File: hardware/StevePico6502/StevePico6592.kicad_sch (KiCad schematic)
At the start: 28 parts, among them J1 Conn_01x16, J2 Conn_01x16, J3 Conn_02x16_Odd_Even, J4 Conn_01x01_Pin, SW1 SW_Push, SW2 SW_Push, U1 65CE02, U2 Pico, U3 74HC595, U4 W65C22NxP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

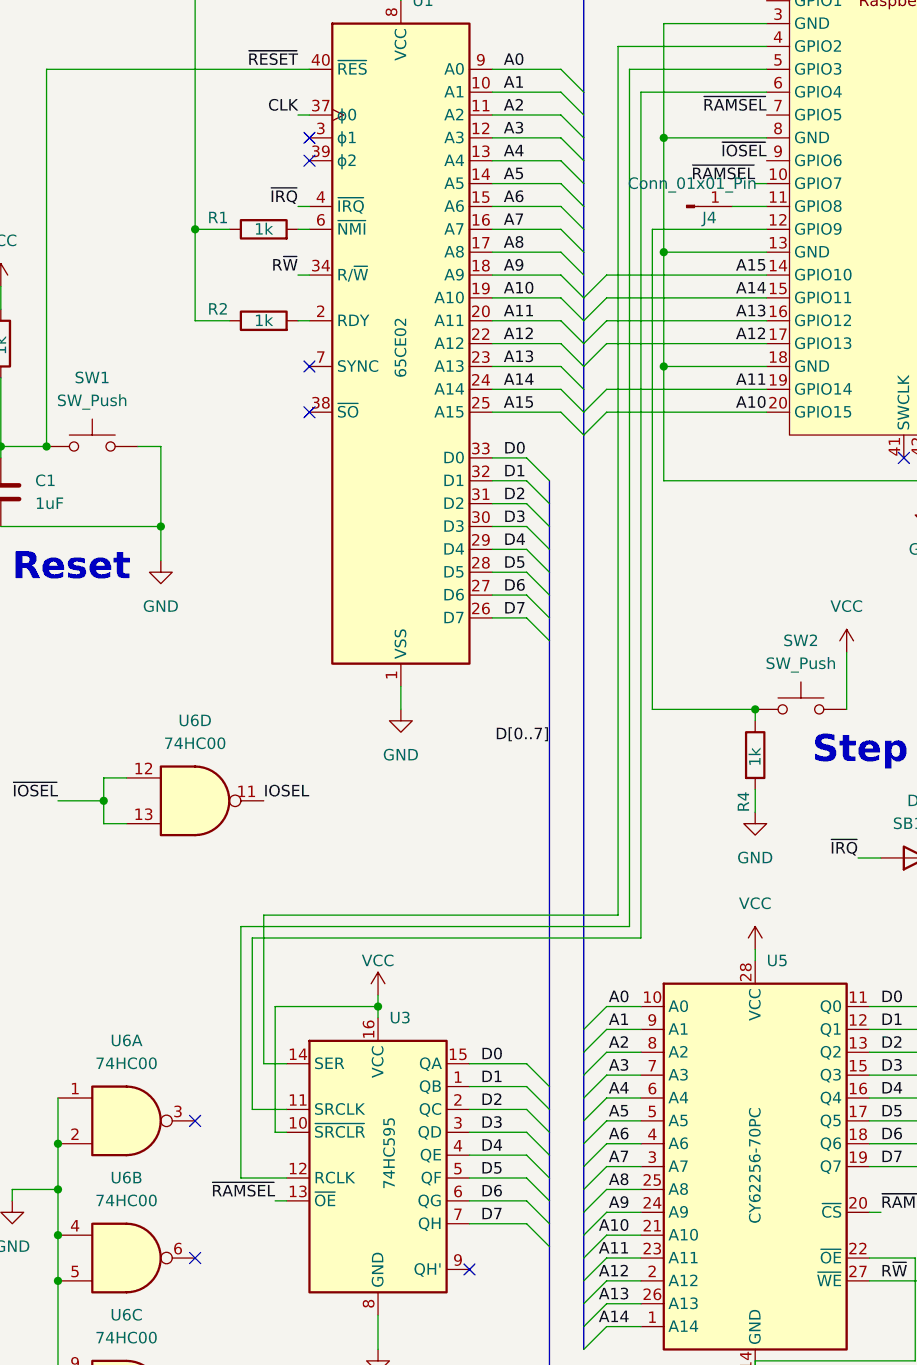
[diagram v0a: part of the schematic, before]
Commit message: fixed bug with dual RAMSEL and no ROMSEL
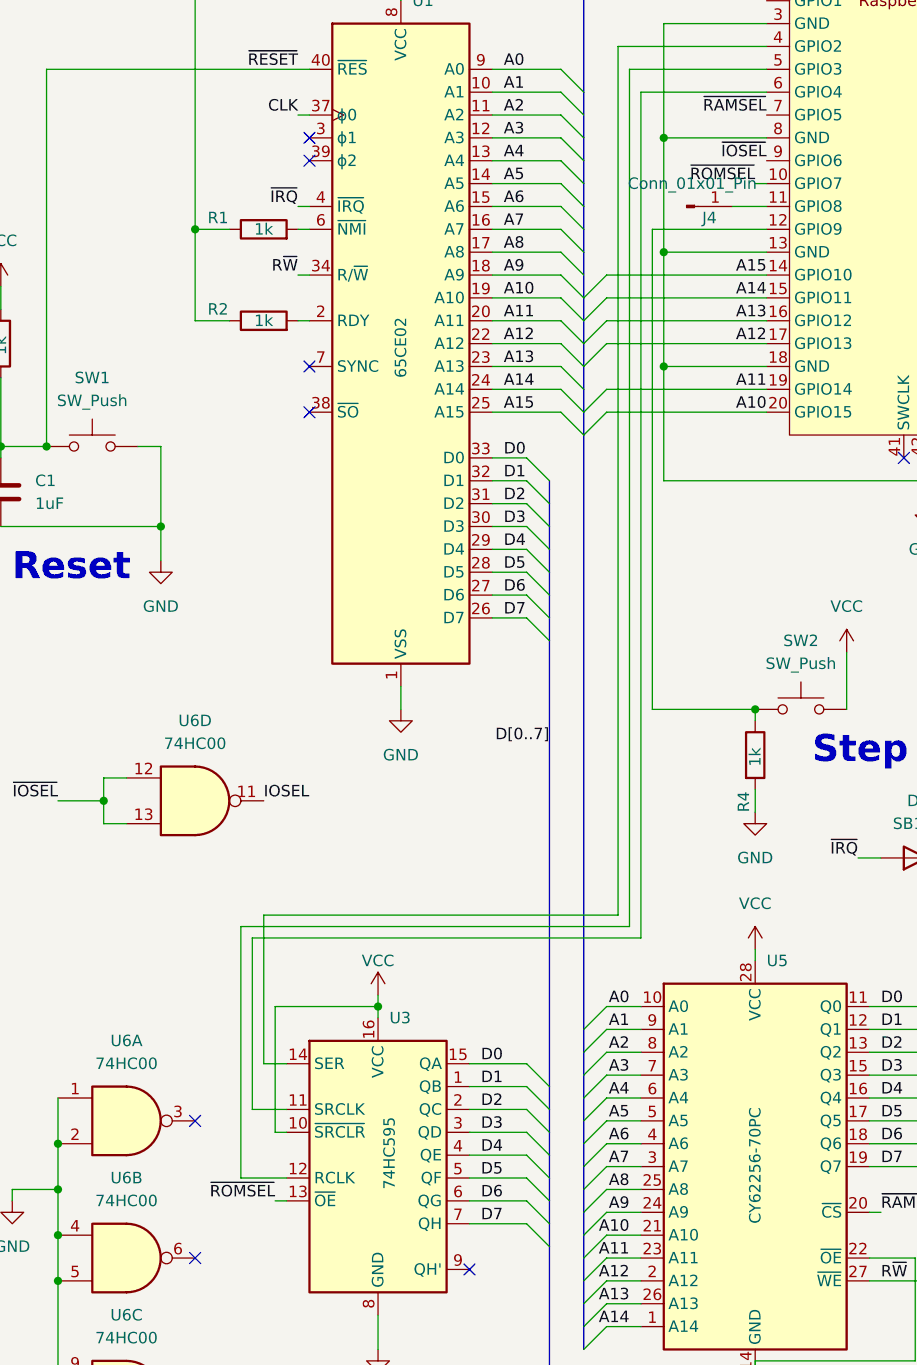
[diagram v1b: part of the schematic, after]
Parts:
- U2: footprint Pi Pico:RPi_Pico_SMD_TH -> MCU_RaspberryPi_and_Boards:RPi_Pico_SMD_TH
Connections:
- net ~{RAMSEL}: no longer U2.10 (GPIO7), U3.13 (~{OE})
- new net ~{ROMSEL}: U2.10 (GPIO7), U3.13 (~{OE})
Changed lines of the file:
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@@
     (effects (font (size 1.27 1.27)) (justify left bottom))
   )
-  (label "~{RAMSEL}" (at 45.72 167.64 180) (fields_autoplaced)
-    (effects (font (size 1.27 1.27)) (justify right bottom))
-  )
-  (label "~{RAMSEL}" (at 99.06 54.61 180) (fields_autoplaced)
+  (label "~{ROMSEL}" (at 45.72 167.64 180) (fields_autoplaced)
+    (effects (font (size 1.27 1.27)) (justify right bottom))
+  )
+  (label "~{ROMSEL}" (at 99.06 54.61 180) (fields_autoplaced)
     (effects (font (size 1.27 1.27)) (justify right bottom))
   )
@@
       (effects (font (size 1.27 1.27)))
     )
-    (property "Footprint" "Pi Pico:RPi_Pico_SMD_TH" (at 118.11 55.88 90)
-      (effects (font (size 1.27 1.27)) hide)
-    )
+    (property "Footprint" "MCU_RaspberryPi_and_Boards:RPi_Pico_SMD_TH" (at 118.11 55.88 90)
+      (effects (font (size 1.27 1.27)) hide)
+    )

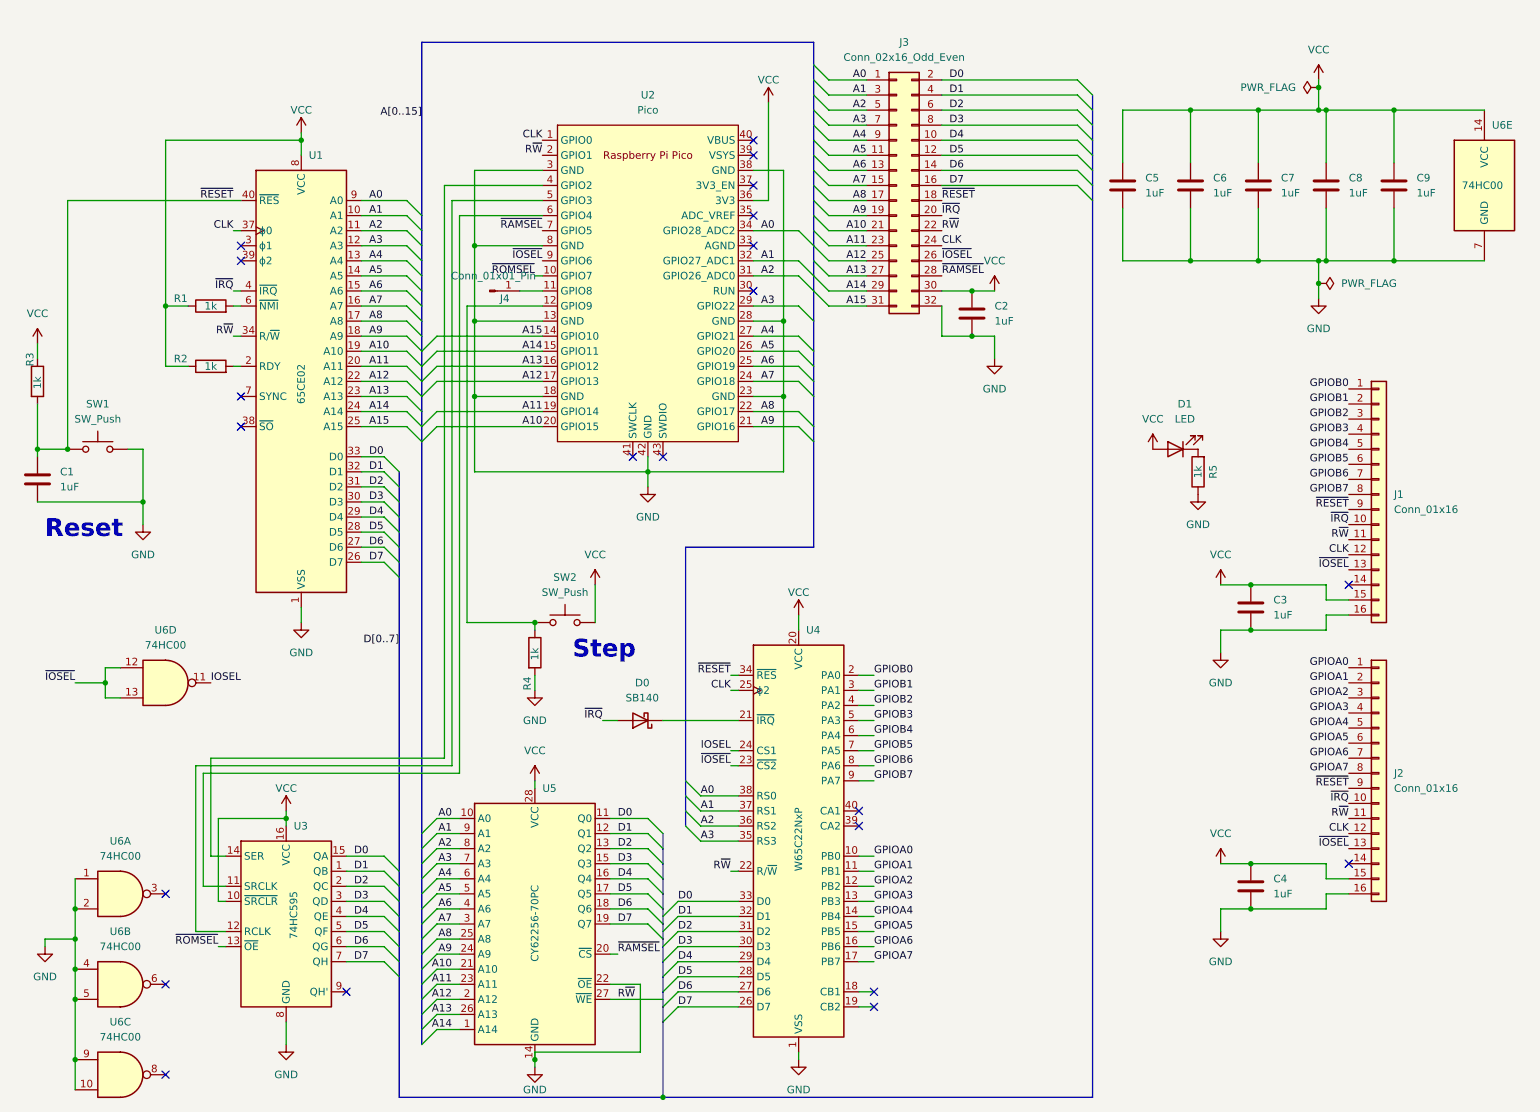
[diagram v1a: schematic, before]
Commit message: V090323 - Removed Pico
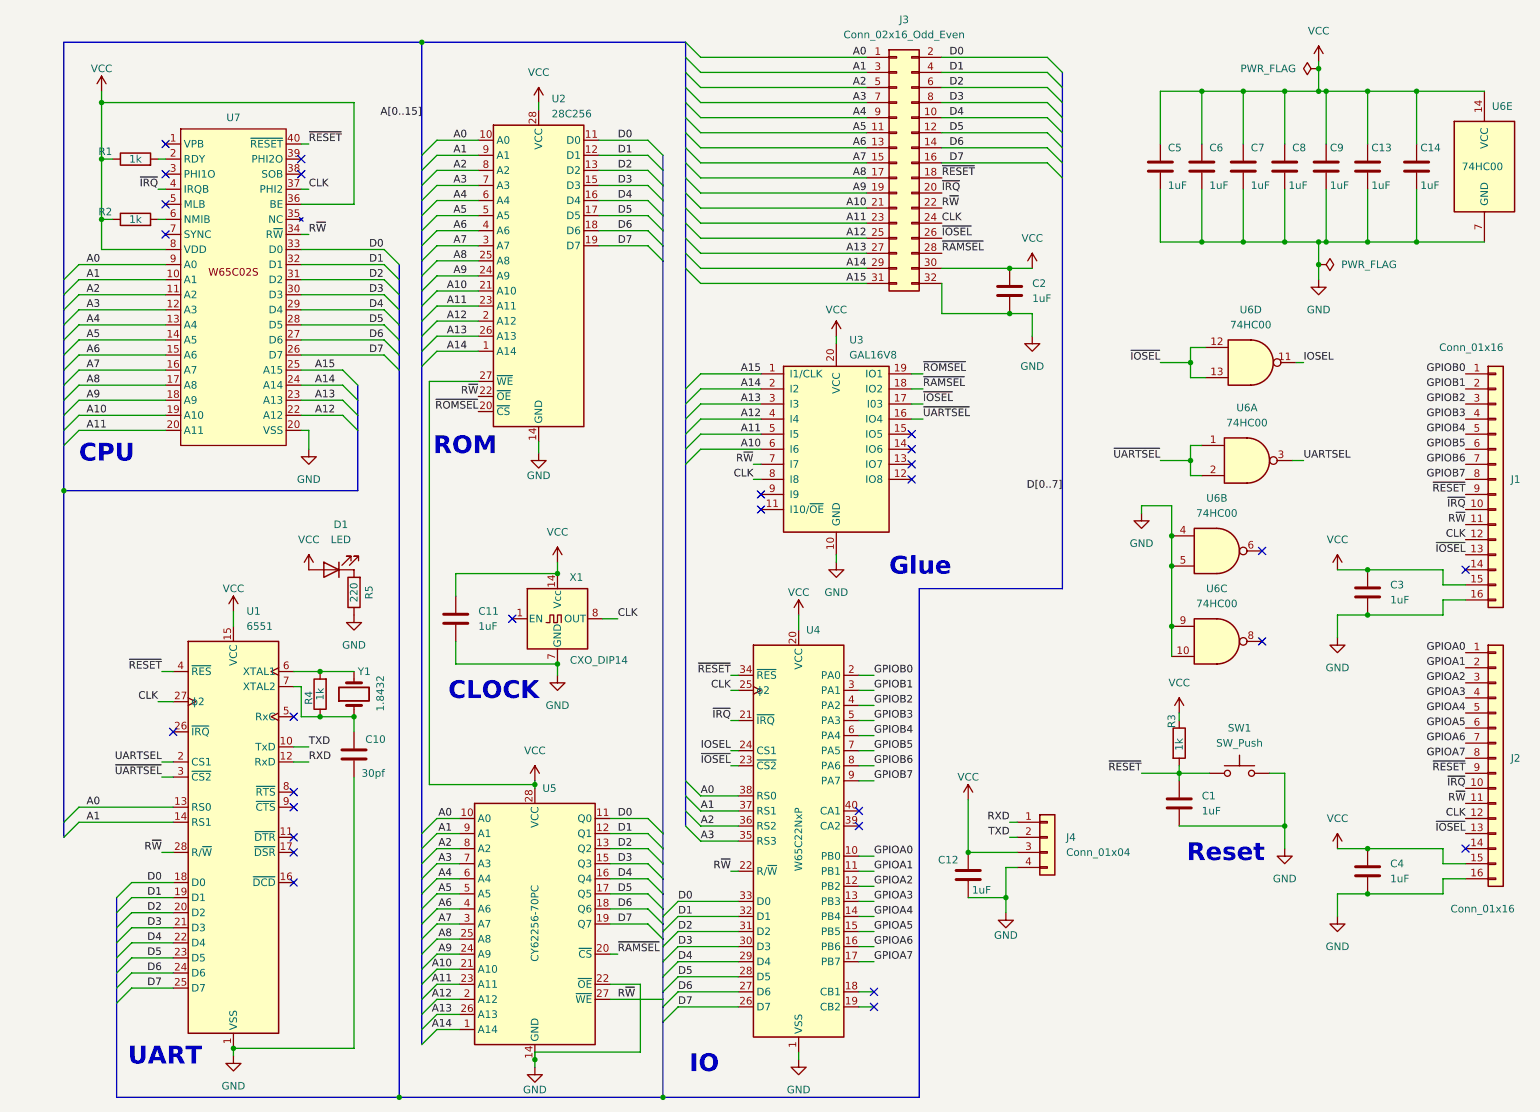
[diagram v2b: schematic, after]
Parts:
- removed D0: SB140, Diode_THT:D_DO-41_SOD81_P10.16mm_Horizontal, symbol Diode:SB140
- removed J4: Conn_01x01_Pin, Connector_PinHeader_2.54mm:PinHeader_1x01_P2.54mm_Vertical, symbol Connector:Conn_01x01_Pin
- removed SW2: SW_Push, Button_Switch_THT:SW_PUSH_6mm, symbol Switch:SW_Push
- removed U1: 65CE02, Package_DIP:DIP-40_W15.24mm, symbol 65xx-library:65CE02
- removed U2: Pico, MCU_RaspberryPi_and_Boards:RPi_Pico_SMD_TH, symbol MCU_RaspberryPi_and_Boards:Pico
- removed U3: 74HC595, Package_DIP:DIP-16_W7.62mm_Socket_LongPads, symbol 74xx:74HC595
- added C10: 30pf, Capacitor_THT:C_Disc_D3.4mm_W2.1mm_P2.50mm, symbol Device:C
- added C11, C12, C13, C14: 1uF, Capacitor_THT:C_Disc_D3.4mm_W2.1mm_P2.50mm, symbol Device:C
- added J4: Conn_01x04, Connector_PinHeader_2.54mm:PinHeader_1x04_P2.54mm_Vertical, symbol Connector_Generic:Conn_01x04
- added U1: 6551, Package_DIP:DIP-28_W15.24mm, symbol 65xx-library:6551
- added U2: 28C256, Package_DIP:DIP-28_W15.24mm_Socket_LongPads, symbol Memory_EEPROM:28C256
- added U3: GAL16V8, Package_DIP:DIP-20_W7.62mm_Socket_LongPads, symbol Logic_Programmable:GAL16V8
- added U7: ~, Package_DIP:DIP-40_W15.24mm_Socket_LongPads, symbol 6502:W65C02S
- added X1: CXO_DIP14, Oscillator:Oscillator_DIP-14, symbol Oscillator:CXO_DIP14
- added Y1: 1.8432, Crystal:Crystal_HC18-U_Vertical, symbol Device:Crystal
- R1, R2, R3, R4: footprint Resistor_THT:R_Axial_DIN0204_L3.6mm_D1.6mm_P5.08mm_Horizontal -> Resistor_THT:R_Axial_DIN0207_L6.3mm_D2.5mm_P7.62mm_Horizontal
- R5: value 1k -> 220; footprint Resistor_THT:R_Axial_DIN0204_L3.6mm_D1.6mm_P5.08mm_Horizontal -> Resistor_THT:R_Axial_DIN0207_L6.3mm_D2.5mm_P7.62mm_Horizontal
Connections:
- net A0: now also U1.13 (RS0), U2.10 (A0), U7.9 (A0)
- net A1: now also U1.14 (RS1), U2.9 (A1), U7.10 (A1)
- net A10: now also U2.21 (A10), U3.6 (I6), U7.19 (A10)
- net A11: now also U2.23 (A11), U3.5 (I5), U7.20 (VSS)
- net A12: now also U2.2 (A12), U3.4 (I4), U7.22 (A12)
- net A13: now also U2.26 (A13), U3.3 (I3), U7.23 (A13)
- net A14: now also U2.1 (A14), U3.2 (I2), U7.24 (A14)
- net A15: now also U3.1 (I1/CLK), U7.25 (A15)
- net A2: now also U2.8 (A2), U7.11 (A2)
- net A3: now also U2.7 (A3), U7.12 (A3)
- net A4: now also U2.6 (A4), U7.13 (A4)
- net A5: now also U2.5 (A5), U7.14 (A5)
- net A6: now also U2.4 (A6), U7.15 (A6)
- net A7: now also U2.3 (A7), U7.16 (A7)
- net A8: now also U2.25 (A8), U7.17 (A8)
- net A9: now also U2.24 (A9), U7.18 (A9)
- net CLK: now also U1.27 (ϕ2), U3.8 (I8), U7.37 (PHI2), X1.8 (OUT)
- net D0: now also U1.18 (D0), U2.11 (D0), U7.33 (D0)
- net D1: now also U1.19 (D1), U2.12 (D1), U7.32 (D1)
- net D2: now also U1.20 (D2), U2.13 (D2), U7.31 (D2)
- net D3: now also U1.21 (D3), U2.15 (D3), U7.30 (D3)
- net D4: now also U1.22 (D4), U2.16 (D4), U7.29 (D4)
- net D5: now also U1.23 (D5), U2.17 (D5), U7.28 (D5)
- net D6: now also U1.24 (D6), U2.18 (D6), U7.27 (D6)
- net D7: now also U1.25 (D7), U2.19 (D7), U7.26 (D7)
- net GND: now also C10.2, C11.2, C12.2, C13.2, C14.2, J4.4 (Pin_4), U1.1 (VSS), U2.14 (GND), U3.10 (GND), U7.20 (VSS), X1.7 (GND); no longer R4.2, U6.1, U6.2
- net R~{W}: now also U1.28 (R/~{W}), U2.22 (~{OE}), U3.7 (I7), U7.34 (R~{W})
- net VCC: now also C11.1, C12.1, C13.1, C14.1, J4.3 (Pin_3), U1.15 (VCC), U2.27 (~{WE}), U2.28 (VCC), U3.20 (VCC), U7.36 (BE), U7.8 (VDD), X1.14 (Vcc)
- net ~{IOSEL}: now also U3.17 (I03)
- net ~{IRQ}: now also U4.21 (~{IRQ}), U7.4 (IRQB)
- net ~{RAMSEL}: now also U3.18 (IO2)
- net ~{RESET}: now also U1.4 (~{RES}), U7.40 (~{RESET})
- net ~{ROMSEL}: now also U2.20 (~{CS}), U3.19 (IO1)
- net at R1.2: now also U7.2 (RDY)
- net at R4.1: now also C10.1, U1.7 (XTAL2), Y1.1
- net at R2.2: now also U7.6 (NMIB)
- net UARTSEL: now reaches U6.3
- net UARTSEL: now also U1.2 (CS1)
- new net: R4.2, U1.6 (XTAL1), Y1.2
- new net RXD: J4.1 (Pin_1), U1.12 (RxD)
- new net TXD: J4.2 (Pin_2), U1.10 (TxD)
- new net ~{UARTSEL}: U1.3 (~{CS2}), U3.16 (IO4), U6.1, U6.2
- no-connect marks 22 -> 28
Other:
- note added: "CLOCK"
- note added: "CPU"
- note added: "Glue"
- note added: "IO"
- note added: "ROM"
- note added: "UART"
- note removed: "Step"
- moved on the sheet: C1, C2, C3, C4, C5, C6, C7, C8, C9, D1, J1, J2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

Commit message: new directio
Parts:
- removed U2: 28C256, Package_DIP:DIP-28_W15.24mm_Socket_LongPads, symbol Memory_EEPROM:28C256
- removed U3: GAL16V8, Package_DIP:DIP-20_W7.62mm_Socket_LongPads, symbol Logic_Programmable:GAL16V8
- removed U7: ~, Package_DIP:DIP-40_W15.24mm_Socket_LongPads, symbol 6502:W65C02S
- added U1: 28C256, symbol Memory_EEPROM:28C256
- added U2: ~, Package_DIP:DIP-40_W15.24mm_Socket_LongPads, symbol 6502:W65C02S
- renumbered U5 to U3, U1 to U4, U4 to U5
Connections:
- net A0: now also U1.10 (A0), U2.9 (A0)
- net A1: now also U1.9 (A1), U2.10 (A1)
- net A10: now also U1.21 (A10), U2.19 (A10)
- net A11: now also U1.23 (A11), U2.20 (A11)
- net A12: now also U1.2 (A12), U2.22 (A12)
- net A13: now also U1.26 (A13), U2.23 (A13)
- net A14: now also U6.10, U1.1 (A14), U2.24 (A14)
- net A15: now also U6.1, U6.2, U2.25 (A15)
- net A2: now also U1.8 (A2), U2.11 (A2)
- net A3: now also U1.7 (A3), U2.12 (A3)
- net A4: now also U1.6 (A4), U2.13 (A4)
- net A5: now also U1.5 (A5), U2.14 (A5)
- net A6: now also U1.4 (A6), U2.15 (A6)
- net A7: now also U1.3 (A7), U2.16 (A7)
- net A8: now also U1.25 (A8), U2.17 (A8)
- net A9: now also U1.24 (A9), U2.18 (A9)
- net CLK: now also U6.5, U2.37 (PHI2)
- net D0: now also U1.11 (D0), U2.33 (D0)
- net D1: now also U1.12 (D1), U2.32 (D1)
- net D2: now also U1.13 (D2), U2.31 (D2)
- net D3: now also U1.15 (D3), U2.30 (D3)
- net D4: now also U1.16 (D4), U2.29 (D4)
- net D5: now also U1.17 (D5), U2.28 (D5)
- net D6: now also U1.18 (D6), U2.27 (D6)
- net D7: now also U1.19 (D7), U2.26 (D7)
- net GND: now also U6.12, U6.13, U1.14 (GND), U2.21 (VSS); no longer U6.10, U6.4, U6.5, U6.9
- net IOSEL: no longer U6.11
- net R~{W}: now also U1.22 (~{OE}), U2.34 (R~{W})
- net UARTSEL: no longer U6.3
- net VCC: now also U1.27 (~{WE}), U1.28 (VCC), U2.36 (BE), U2.8 (VDD)
- net ~{IOSEL}: now also U6.8; no longer U6.12, U6.13
- net ~{IRQ}: now also U2.4 (IRQB)
- net ~{RAMSEL}: now also U6.6
- net ~{RESET}: now also U2.40 (~{RESET})
- net ~{ROMSEL}: now also U6.3, U6.4, U6.9, U1.20 (~{CS})
- net ~{UARTSEL}: no longer U6.1, U6.2
- net at R1.2: now also U2.2 (RDY)
- net at R2.2: now also U2.6 (NMIB)
- no-connect marks 28 -> 21
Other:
- note removed: "Glue"
- note removed: "ROM"
- moved on the sheet: C1, C12, C13, C14, C2, C5, C6, C7, C8, C9, D1, J3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
